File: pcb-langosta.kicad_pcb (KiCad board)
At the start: 2 copper layers, 41 x 80 mm, 2 parts

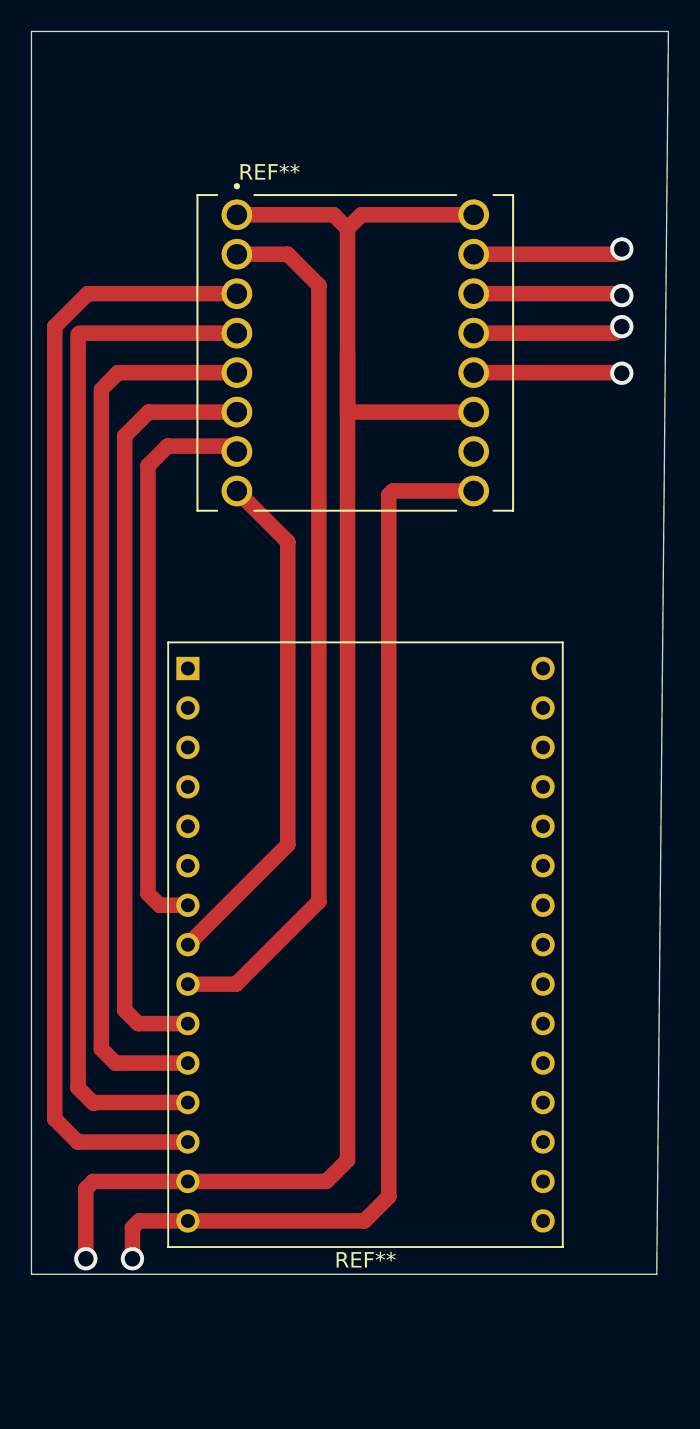
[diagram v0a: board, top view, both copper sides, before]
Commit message: feat: agregando switch
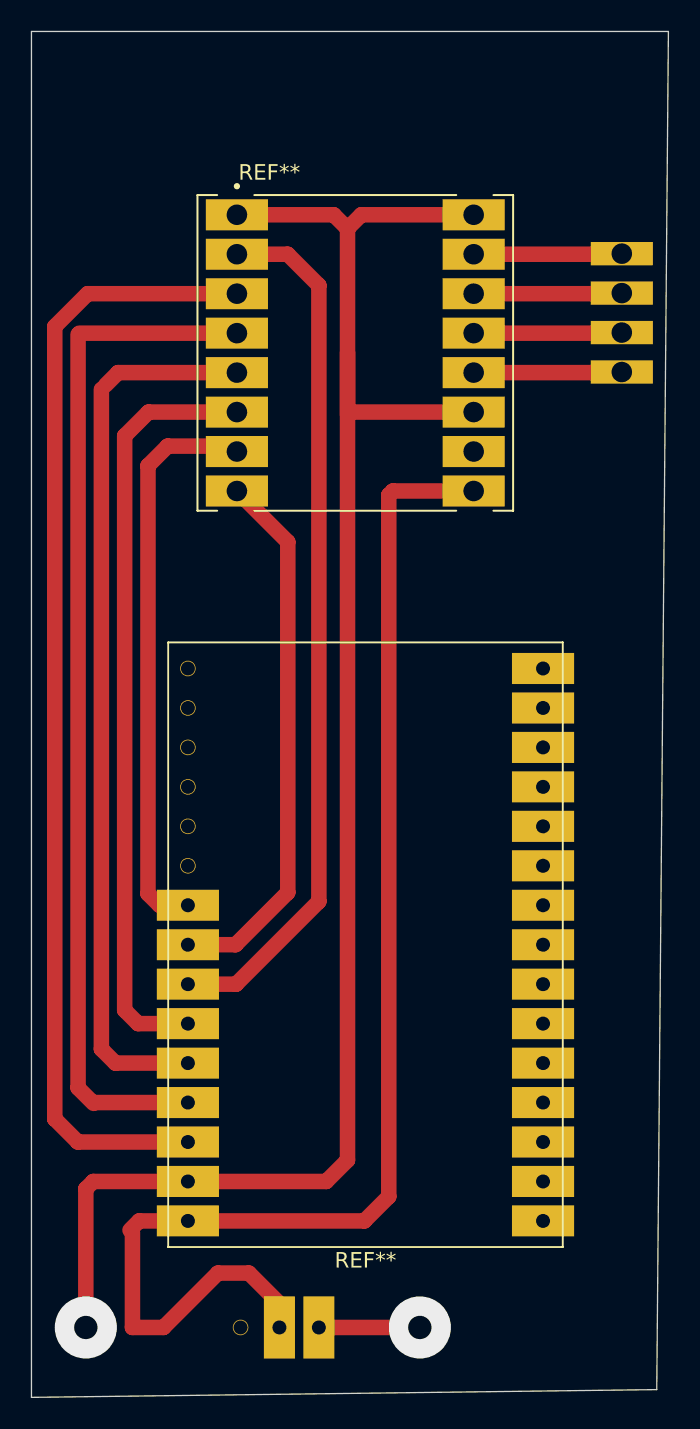
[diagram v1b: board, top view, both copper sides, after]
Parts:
- added ?: , , F.Cu at (59.0, 30.9)
- added ?: , , F.Cu at (59.0, 28.4)
- added ?: , , F.Cu at (59.0, 36.0)
- added ?: , , F.Cu at (37.0, 97.5)
- added ?: , , F.Cu at (59.0, 33.5)
- added ?: , , F.Cu at (39.5, 97.5)
- added ?: , , F.Cu at (34.5, 97.5)
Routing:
- net (no net): track 591.2 -> 621.1 mm, vias 6 -> 2
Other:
- board size 41 x 80 mm -> 41 x 87.9 mm
